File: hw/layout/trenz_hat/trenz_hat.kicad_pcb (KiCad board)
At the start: 2 copper layers, 104 parts

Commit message: Implement internal Pi FPGA link and remove ribbon expansion
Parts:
- removed J84: , elec:TZ_TZ_JTAG
- removed J85: , elec:TZ_TZ_AUX
- removed J86, J87: , elec:TZ_FFC40
- removed J88, J89: , elec:TZ_FFC60
- added C100: , elec:Capacitor_SMD__C_0603_1608Metric, F.Cu at (60.0, 0.00)
- added C101: , elec:Capacitor_SMD__C_0603_1608Metric, F.Cu at (70.0, 0.00)
- added C102: , elec:Capacitor_SMD__C_0603_1608Metric, F.Cu at (80.0, 0.00)
- added C103: , elec:Capacitor_SMD__C_0603_1608Metric, F.Cu at (90.0, 0.00)
- added C104: , elec:Capacitor_SMD__C_0603_1608Metric, F.Cu at (100.0, 0.00)
- added C105: , elec:Capacitor_SMD__C_0603_1608Metric, F.Cu at (110.0, 0.00)
- added C106: , elec:Capacitor_SMD__C_0603_1608Metric, F.Cu at (10.0, 0.00)
- added R100: , elec:Resistor_SMD__R_0603_1608Metric, F.Cu at (120.0, 0.00)
- added R101: , elec:Resistor_SMD__R_0603_1608Metric, F.Cu at (130.0, 0.00)
- added R102: , elec:Resistor_SMD__R_0603_1608Metric, F.Cu at (140.0, 0.00)
- added R103: , elec:Resistor_SMD__R_0603_1608Metric, F.Cu at (150.0, 0.00)
- added R104: , elec:Resistor_SMD__R_0603_1608Metric, F.Cu at (160.0, 0.00)
- added R105: , elec:Resistor_SMD__R_0603_1608Metric, F.Cu at (170.0, 0.00)
- added R106: , elec:Resistor_SMD__R_0603_1608Metric, F.Cu at (180.0, 0.00)
- added R107: , elec:Resistor_SMD__R_0603_1608Metric, F.Cu at (190.0, 0.00)
- added R108: , elec:Resistor_SMD__R_0603_1608Metric, F.Cu at (200.0, 0.00)
- added R109: , elec:Resistor_SMD__R_0603_1608Metric, F.Cu at (210.0, 0.00)
- added R110: , elec:Resistor_SMD__R_0603_1608Metric, F.Cu at (220.0, 0.00)
- added R111: , elec:Resistor_SMD__R_0603_1608Metric, F.Cu at (230.0, 0.00)
- added R112: , elec:Resistor_SMD__R_0603_1608Metric, F.Cu at (240.0, 0.00)
- added R113: , elec:Resistor_SMD__R_0603_1608Metric, F.Cu at (250.0, 0.00)
- added R114: , elec:Resistor_SMD__R_0603_1608Metric, F.Cu at (260.0, 0.00)
- added R115: , elec:Resistor_SMD__R_0603_1608Metric, F.Cu at (270.0, 0.00)
- added R116: , elec:Resistor_SMD__R_0603_1608Metric, F.Cu at (280.0, 0.00)
- added R117: , elec:Resistor_SMD__R_0603_1608Metric, F.Cu at (290.0, 0.00)
- added U100: , elec:Package_SO__TSSOP-16_4.4x5mm_P0.65mm, F.Cu at (0.00, 0.00)
- added U101: , elec:Package_SO__TSSOP-16_4.4x5mm_P0.65mm, F.Cu at (10.0, 0.00)
- added U102: , elec:Package_SO__TSSOP-16_4.4x5mm_P0.65mm, F.Cu at (20.0, 0.00)
- added U103: , elec:Package_TO_SOT_SMD__SOT-363_SC-70-6, F.Cu at (30.0, 0.00)
- added U104: , elec:Package_TO_SOT_SMD__SOT-23, F.Cu at (40.0, 0.00)
- added U105: , elec:Package_TO_SOT_SMD__SOT-23, F.Cu at (50.0, 0.00)
- added U106: , elec:Package_TO_SOT_SMD__SOT-353_SC-70-5, F.Cu at (0.00, 0.00)
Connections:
- J1 pad 12: 12 -> PI_LINK_CS_N
- J1 pad 32: 32 -> PI_LINK_DQ3
- J1 pad 35: 35 -> PI_LINK_DQ1
- J1 pad 36: 36 -> PI_LINK_DQ2
- J1 pad 38: 38 -> PI_LINK_DQ0
- J1 pad 40: 40 -> PI_LINK_SCLK
- J80 pad 100: FPGA_B14_L24_N -> 100
- J80 pad 15: FPGA_B13_L6_N -> 15
- J80 pad 17: FPGA_B13_L6_P -> 17
- J80 pad 18: FPGA_B13_L3_P -> 18
- J80 pad 20: FPGA_B13_L3_N -> 20
- J80 pad 21: FPGA_B13_L5_N -> 21
- J80 pad 22: FPGA_B13_L11_N -> 22
- J80 pad 23: FPGA_B13_L5_P -> 23
- J80 pad 24: FPGA_B13_L11_P -> 24
- J80 pad 26: FPGA_B13_L9_N -> 26
- J80 pad 28: FPGA_B13_L9_P -> 28
- J80 pad 32: FPGA_B16_L22_P -> 32
- J80 pad 34: FPGA_B16_L22_N -> 34
- J80 pad 35: FPGA_B16_L16_P -> 35
- J80 pad 36: FPGA_B16_L24_N -> 36
- J80 pad 37: FPGA_B16_L16_N -> 37
- J80 pad 38: FPGA_B16_L24_P -> 38
- J80 pad 39: FPGA_B16_L19_N -> 39
- J80 pad 40: j80-40 -> 40
- J80 pad 41: FPGA_B16_L19_P -> 41
- J80 pad 42: FPGA_B16_L23_P -> 42
- J80 pad 44: FPGA_B16_L23_N -> 44
- J80 pad 45: FPGA_B16_L17_N -> 45
- J80 pad 46: FPGA_B16_L15_P -> 46
- J80 pad 47: FPGA_B16_L17_P -> 47
- J80 pad 48: FPGA_B16_L15_N -> 48
- J80 pad 49: FPGA_B16_L18_N -> 49
- J80 pad 50: FPGA_B16_L20_P -> 50
- J80 pad 51: FPGA_B16_L18_P -> 51
- J80 pad 52: FPGA_B16_L20_N -> 52
- J80 pad 55: FPGA_B16_L9_N -> 55
- J80 pad 56: FPGA_B16_L21_P -> 56
- J80 pad 57: FPGA_B16_L9_P -> 57
- J80 pad 58: FPGA_B16_L21_N -> 58
- J80 pad 59: FPGA_B16_L7_N -> 59
- J80 pad 60: FPGA_B16_L13_P -> 60
- J80 pad 61: FPGA_B16_L7_P -> 61
- J80 pad 62: FPGA_B16_L13_N -> 62
- J80 pad 65: FPGA_B16_L11_P -> 65
- J80 pad 66: FPGA_B16_L14_P -> 66
- J80 pad 67: FPGA_B16_L11_N -> 67
- J80 pad 68: FPGA_B16_L14_N -> 68
- J80 pad 69: FPGA_B16_L10_N -> 69
- J80 pad 70: FPGA_B16_L3_N -> 70
- J80 pad 71: FPGA_B16_L10_P -> 71
- J80 pad 72: FPGA_B16_L3_P -> 72
- J80 pad 75: FPGA_B16_L5_N -> 75
- J80 pad 76: FPGA_B16_L12_P -> 76
- J80 pad 77: FPGA_B16_L5_P -> 77
- J80 pad 78: FPGA_B16_L12_N -> 78
- J80 pad 79: FPGA_B16_L2_N -> 79
- J80 pad 81: FPGA_B16_L2_P -> 81
- J80 pad 82: FPGA_B16_L8_N -> 82
- J80 pad 84: FPGA_B16_L8_P -> 84
- J80 pad 85: FPGA_B16_L6_N -> 85
- J80 pad 86: FPGA_B14_L18_N -> 86
- J80 pad 87: FPGA_B16_L6_P -> 87
- J80 pad 88: FPGA_B14_L18_P -> 88
- J80 pad 91: FPGA_B14_L24_P -> 91
- J80 pad 92: FPGA_B14_L9_P -> 92
- J80 pad 93: FPGA_B16_L4_N -> 93
- J80 pad 94: FPGA_B14_L9_N -> 94
- J80 pad 95: FPGA_B16_L4_P -> 95
- J80 pad 96: FPGA_B14_L4_P -> 96
- J80 pad 97: FPGA_B16_L1_N -> 97
- J80 pad 98: FPGA_B14_L4_N -> 98
- J80 pad 99: FPGA_B16_L1_P -> 99
- J81 pad 15: FPGA_AUX0 -> j81-15
- J81 pad 16: FPGA_AUX1 -> 16
- J81 pad 18: FPGA_AUX2 -> j81-18
- J81 pad 20: 20 -> j81-20
- J81 pad 21: FPGA_B14_L12_P -> FPGA_LINK_SCLK
- J81 pad 22: FPGA_B14_L14_P -> FPGA_LINK_DQ0
- J81 pad 23: FPGA_B14_L12_N -> FPGA_LINK_CS_N
- J81 pad 24: FPGA_B14_L14_N -> FPGA_LINK_DQ1
- J81 pad 25: FPGA_B14_L11_P -> 25
- J81 pad 26: FPGA_B14_L13_P -> FPGA_LINK_DQ2
- J81 pad 27: FPGA_B14_L11_N -> 27
- J81 pad 28: FPGA_B14_L13_N -> FPGA_LINK_DQ3
- J81 pad 31: FPGA_B15_L9_N -> 31
- J81 pad 32: FPGA_B14_L16_P -> j81-32
- J81 pad 33: FPGA_B15_L9_P -> 33
- J81 pad 34: FPGA_B14_L16_N -> j81-34
- J81 pad 35: FPGA_B15_L8_N -> j81-35
- J81 pad 36: FPGA_B14_L15_P -> j81-36
- J81 pad 37: FPGA_B15_L8_P -> j81-37
- J81 pad 38: FPGA_B14_L15_N -> j81-38
- J81 pad 41: FPGA_B15_L7_N -> j81-41
- J81 pad 42: FPGA_B15_L23_P -> j81-42
- J81 pad 43: FPGA_B15_L7_P -> 43
- J81 pad 44: FPGA_B15_L23_N -> j81-44
- J81 pad 45: FPGA_B15_L13_P -> j81-45
- J81 pad 46: FPGA_B15_L19_P -> j81-46
- J81 pad 47: FPGA_B15_L13_N -> j81-47
- J81 pad 48: FPGA_B15_L19_N -> j81-48
- J81 pad 51: FPGA_B15_L14_P -> j81-51
- J81 pad 52: FPGA_B15_L11_P -> j81-52
- J81 pad 53: FPGA_B15_L14_N -> 53
- J81 pad 54: FPGA_B15_L11_N -> 54
- J81 pad 55: FPGA_B15_L12_P -> j81-55
- J81 pad 56: FPGA_B15_L3_P -> j81-56
- J81 pad 57: FPGA_B15_L12_N -> j81-57
- J81 pad 58: FPGA_B15_L3_N -> j81-58
- J81 pad 61: FPGA_B15_L10_N -> j81-61
- J81 pad 62: FPGA_B15_L17_N -> j81-62
- J81 pad 63: FPGA_B15_L10_P -> 63
- J81 pad 64: FPGA_B15_L17_P -> 64
- J81 pad 65: FPGA_B15_L18_P -> j81-65
- J81 pad 66: FPGA_B15_L16_P -> j81-66
- J81 pad 67: FPGA_B15_L18_N -> j81-67
- J81 pad 68: FPGA_B15_L16_N -> j81-68
- J81 pad 71: FPGA_B15_L20_P -> j81-71
- J81 pad 72: FPGA_B15_L1_P -> j81-72
- J81 pad 73: FPGA_B15_L20_N -> 73
- J81 pad 74: FPGA_B15_L1_N -> 74
- J81 pad 75: FPGA_B15_L15_P -> j81-75
- J81 pad 76: FPGA_B15_L2_N -> j81-76
- J81 pad 77: FPGA_B15_L15_N -> j81-77
- J81 pad 78: FPGA_B15_L2_P -> j81-78
- J81 pad 81: FPGA_B15_L6_N -> j81-81
- J81 pad 82: FPGA_B15_L4_P -> j81-82
- J81 pad 83: FPGA_B15_L6_P -> 83
- J81 pad 84: FPGA_B15_L4_N -> j81-84
- J81 pad 85: FPGA_B15_L21_P -> j81-85
- J81 pad 86: FPGA_B15_L5_N -> j81-86
- J81 pad 87: FPGA_B15_L21_N -> j81-87
- J81 pad 88: FPGA_B15_L5_P -> j81-88
- J81 pad 90: FPGA_B15_IO0 -> 90
- J81 pad 91: FPGA_B15_L24_N -> j81-91
- J81 pad 93: FPGA_B15_L24_P -> j81-93
- J81 pad 95: FPGA_B15_L22_N -> j81-95
- J81 pad 97: FPGA_B15_L22_P -> j81-97
- J81 pad 99: FPGA_B15_IO25 -> j81-99
- J82 pad 1: FPGA_B13_L14_P -> 1
- J82 pad 15: 15 -> j82-15
- J82 pad 16: 16 -> j82-16
- J82 pad 2: FPGA_B13_L17_P -> 2
- J82 pad 21: 21 -> j82-21
- J82 pad 22: 22 -> j82-22
- J82 pad 25: 25 -> j82-25
- J82 pad 26: 26 -> j82-26
- J82 pad 27: 27 -> j82-27
- J82 pad 28: 28 -> j82-28
- J82 pad 3: FPGA_B13_L14_N -> j82-3
- J82 pad 31: 31 -> j82-31
- J82 pad 33: 33 -> j82-33
- J82 pad 34: 34 -> j82-34
- J82 pad 37: FPGA_B13_L16_P -> j82-37
- J82 pad 38: FPGA_B13_L10_P -> j82-38
- J82 pad 39: FPGA_B13_L16_N -> j82-39
- J82 pad 4: FPGA_B13_L17_N -> 4
- J82 pad 40: FPGA_B13_L10_N -> j82-40
- J82 pad 41: FPGA_B13_L1_P -> j82-41
- J82 pad 42: FPGA_B13_L15_P -> j82-42
- J82 pad 43: FPGA_B13_L1_N -> j82-43
- J82 pad 44: FPGA_B13_L15_N -> j82-44
- J82 pad 47: FPGA_B13_L4_P -> j82-47
- J82 pad 48: FPGA_B14_L5_P -> j82-48
- J82 pad 49: FPGA_B13_L4_N -> j82-49
- J82 pad 50: FPGA_B14_L5_N -> j82-50
- J82 pad 51: FPGA_B13_L2_N -> j82-51
- J82 pad 52: FPGA_B14_L20_P -> j82-52
- J82 pad 53: FPGA_B13_L2_P -> j82-53
- J82 pad 54: FPGA_B14_L20_N -> j82-54
- J82 pad 55: 55 -> j82-55
- J82 pad 56: 56 -> j82-56
- J82 pad 57: FPGA_B13_L12_P -> j82-57
- J82 pad 58: FPGA_B13_L13_P -> j82-58
- J82 pad 59: FPGA_B13_L12_N -> j82-59
- J82 pad 60: FPGA_B13_L13_N -> j82-60

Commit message: Rename project to Groundlark and sensor carrier to DAQHAT-01
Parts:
- U20: footprint elec:ShakeSense__SCL3300_D01 -> elec:Groundlark__SCL3300_D01
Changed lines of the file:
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@@
 		)
 	)
-	(footprint "elec:ShakeSense__SCL3300_D01"
+	(footprint "elec:Groundlark__SCL3300_D01"
 		(layer "F.Cu")
 		(at 250 0 0)

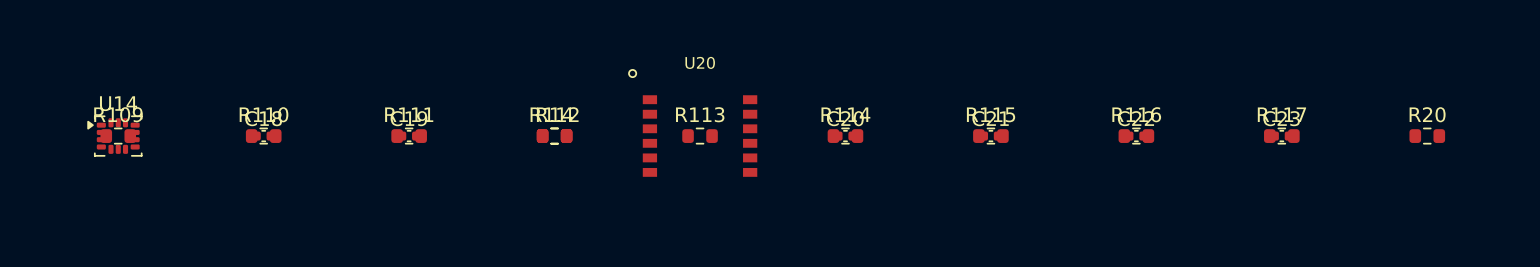
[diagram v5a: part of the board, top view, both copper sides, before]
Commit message: Harden DAQHAT-01 assembly exports and refresh stack overview
Publish the current three-IMU six-layer revision and matching software. Capture exact-part sourcing, shortage substitutions and numbered-pad rotation mappings with regression and full/overlay integration tests. Preserve validated BOM bytes across Git checkouts. Replace README images with the current stack and a dimensioned geophone illustration; keep fabrication packages local.
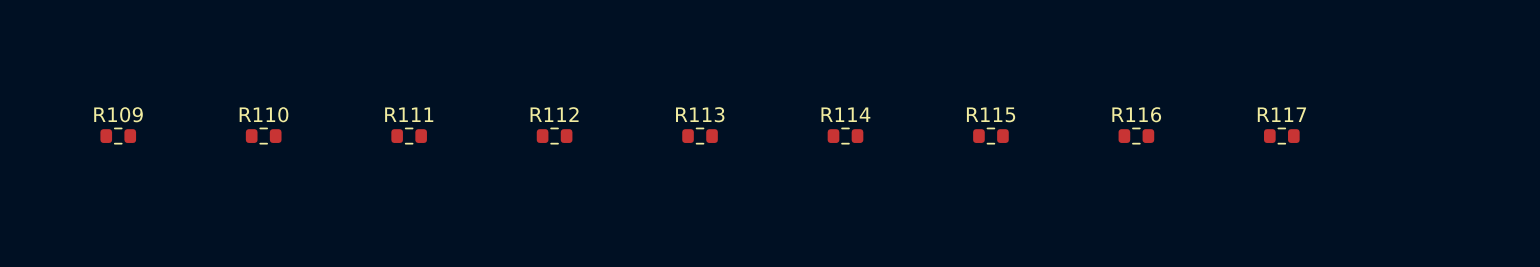
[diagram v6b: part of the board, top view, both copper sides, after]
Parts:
- removed C18, C19, C20, C21, C22, C23: , elec:Capacitor_SMD__C_0402_1005Metric
- removed R14, R20: , elec:Resistor_SMD__R_0603_1608Metric
- removed U14: , elec:Package_LGA__LGA-14_3x2.5mm_P0.5mm_LayoutBorder3x4y
- removed U20: , elec:Groundlark__SCL3300_D01
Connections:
- J1 pad 18: PI_IMU4_INT -> 18
- J1 pad 31: PI_IMU4_CS -> 31
- J1 pad 33: PI_TILT_CS -> 33
- J80 pad 18: 18 -> j80-18
- J81 pad 31: 31 -> j81-31
- J81 pad 33: 33 -> j81-33
- U41 pad 15: TILT_CS -> u41-15
- U41 pad 16: IMU4_CS -> u41-16
- U41 pad 8: PI_IMU4_CS -> GND
- U41 pad 9: PI_TILT_CS -> GND
- U42 pad 17: IMU4_INT -> GND
- U42 pad 7: PI_IMU4_INT -> u42-7
